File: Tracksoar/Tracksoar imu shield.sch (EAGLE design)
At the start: 12 parts, among them U1 HEX_CONVERTER, U2 LSM9DS1

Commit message: removed old shields
removed square shields and added values to shield passives
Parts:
- C1: value (none) -> 10uf
- C2, C3, C5: value (none) -> .1uf
- C4: value (none) -> 10nf
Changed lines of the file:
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@@
 <part name="U1" library="SparkFun-DigitalIC" deviceset="HEX_CONVERTER" device=""/>
 <part name="U2" library="SparkFun-Sensors" deviceset="LSM9DS1" device=""/>
-<part name="C1" library="SparkFun-Passives" deviceset="CAP" device="0805"/>
-<part name="C2" library="SparkFun-Passives" deviceset="CAP" device="0805"/>
-<part name="C3" library="SparkFun-Passives" deviceset="CAP" device="0805"/>
-<part name="C4" library="SparkFun-Passives" deviceset="CAP" device="0805"/>
-<part name="C5" library="SparkFun-Passives" deviceset="CAP" device="0805"/>
+<part name="C1" library="SparkFun-Passives" deviceset="CAP" device="0805" value="10uf"/>
+<part name="C2" library="SparkFun-Passives" deviceset="CAP" device="0805" value=".1uf"/>
+<part name="C3" library="SparkFun-Passives" deviceset="CAP" device="0805" value=".1uf"/>
+<part name="C4" library="SparkFun-Passives" deviceset="CAP" device="0805" value="10nf"/>
+<part name="C5" library="SparkFun-Passives" deviceset="CAP" device="0805" value=".1uf"/>
 <part name="U$2" library="SparkFun-PowerIC" deviceset="LM3480IM4" device=""/>
 </parts>
@@
 <junction x="63.5" y="60.96"/>
 <pinref part="C5" gate="G$1" pin="2"/>
-<wire x1="71.12" y1="60.96" x2="73.66" y2="60.96" width="0.1524" layer="91"/>
+<wire x1="71.12" y1="60.96" x2="78.74" y2="60.96" width="0.1524" layer="91"/>
 <junction x="71.12" y="60.96"/>
 <junction x="40.64" y="60.96"/>
-<label x="73.66" y="60.96" size="1.778" layer="95"/>
+<label x="78.74" y="60.96" size="1.778" layer="95"/>
 </segment>
 </net>

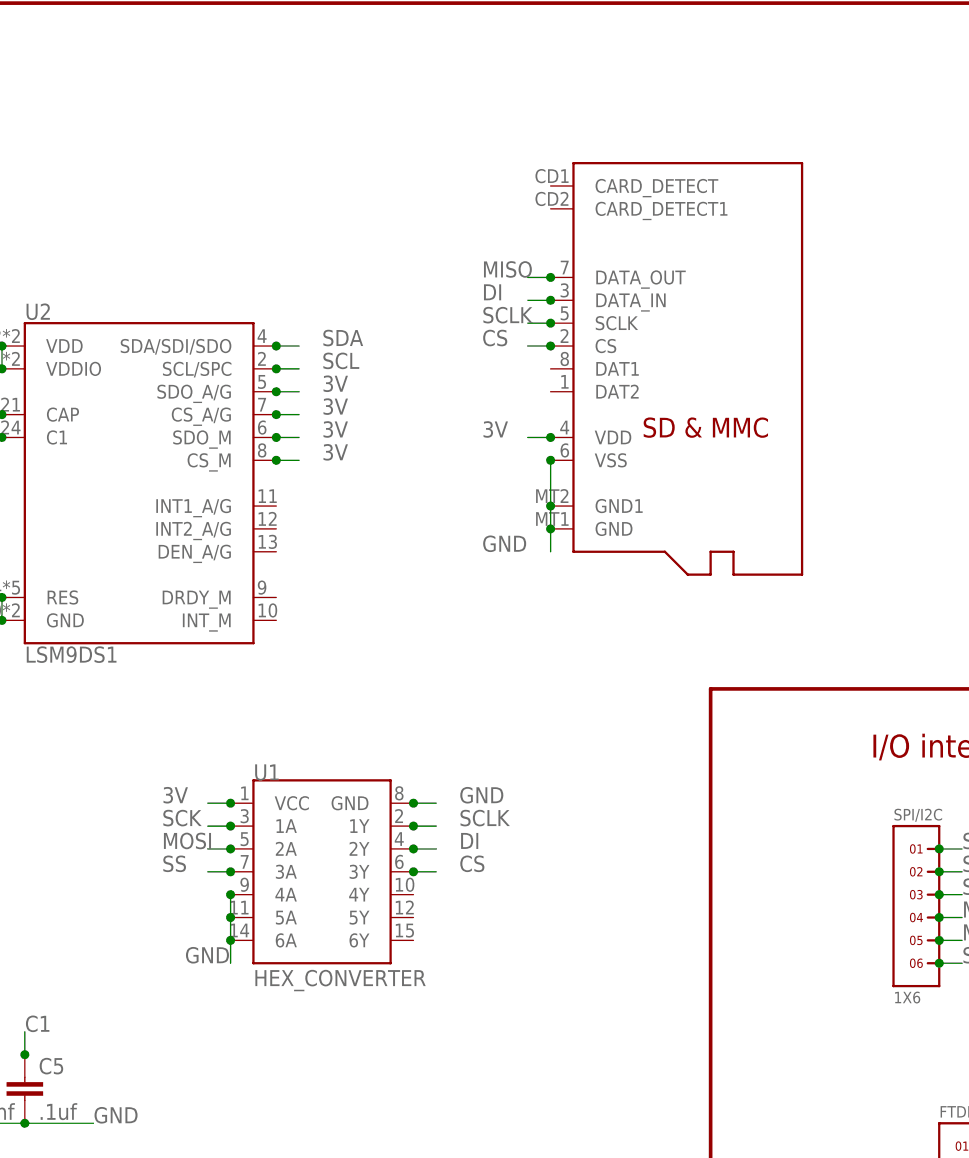
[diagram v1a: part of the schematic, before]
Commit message: replaced sd with eeprom
the atmega328p does not have enough SRAM to handle the Trackuino duties
and SD read / write. It has been replace with an ST Micro M24M02 2Mb
eeprom. This will result in much less RAM usage, a smaller BOM, lower
cost, and lower power usage. However it also means we lose portability
of storage and easy computer interfacing. We’ll look at revising this
in future versions.
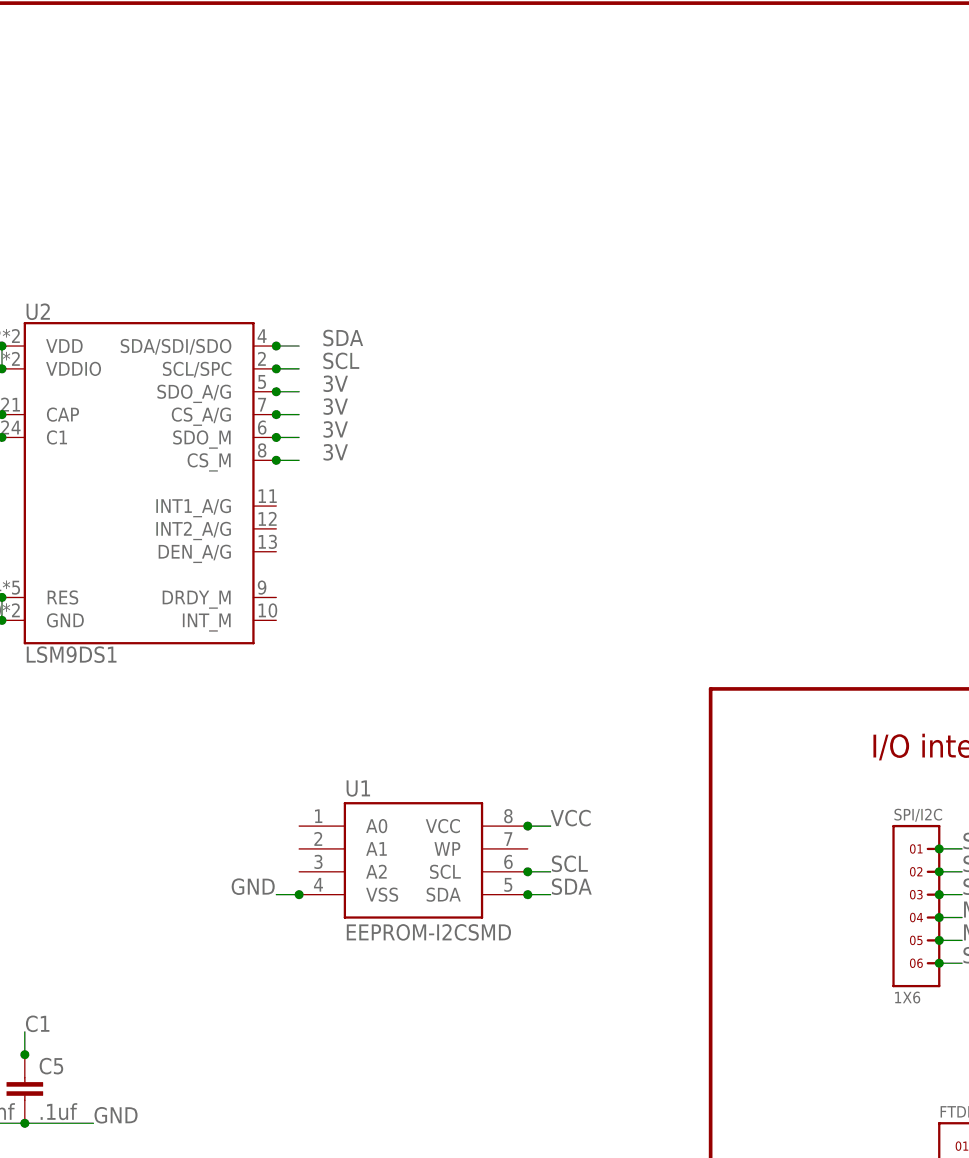
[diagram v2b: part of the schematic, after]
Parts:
- removed U$1: MICROSD, adafruit:MICROSD
- U1: value HEX_CONVERTER -> EEPROM-I2CSMD; device SparkFun-DigitalIC:HEX_CONVERTER -> SparkFun-DigitalIC:EEPROM-I2CSMD
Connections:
- removed net CS: U$1.CS, U1.3Y
- removed net DI: U$1.DATA_IN, U1.2Y
- removed net SCLK: U$1.SCLK, U1.1Y
- net 3V: no longer U$1.VDD, U1.VCC
- net GND: now also U1.VSS; no longer U$1.GND, U$1.GND1, U$1.VSS, U1.4A, U1.5A, U1.6A, U1.GND
- net MISO: no longer U$1.DATA_OUT
- net MOSI: no longer U1.2A
- net SCK: no longer U1.1A
- net SCL: now also U1.SCL
- net SDA: now also U1.SDA
- net SS: no longer U1.3A
- net VCC: now also U1.VCC
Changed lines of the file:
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@@
 <layers>
 <layer number="1" name="Top" color="4" fill="1" visible="no" active="no"/>
+<layer number="2" name="Route2" color="1" fill="3" visible="no" active="no"/>
+<layer number="3" name="Route3" color="4" fill="3" visible="no" active="no"/>
+<layer number="14" name="Route14" color="1" fill="6" visible="no" active="no"/>
+<layer number="15" name="Route15" color="4" fill="6" visible="no" active="no"/>
 <layer number="16" name="Bottom" color="1" fill="1" visible="no" active="no"/>
 <layer number="17" name="Pads" color="2" fill="1" visible="no" active="no"/>
@@
 <part name="FTDI" library="headers(2mm)" deviceset="1X7" device=""/>
 <part name="SPI/I2C" library="headers(2mm)" deviceset="1X6" device=""/>
-<part name="U$1" library="adafruit" deviceset="MICROSD" device=""/>
-<part name="U1" library="SparkFun-DigitalIC" deviceset="HEX_CONVERTER" device=""/>
 <part name="U2" library="SparkFun-Sensors" deviceset="LSM9DS1" device=""/>
 <part name="C1" library="SparkFun-Passives" deviceset="CAP" device="0805" value="10uf"/>
@@
 <part name="C5" library="SparkFun-Passives" deviceset="CAP" device="0805" value=".1uf"/>
 <part name="U$2" library="SparkFun-PowerIC" deviceset="LM3480IM4" device=""/>
+<part name="U1" library="SparkFun-DigitalIC" deviceset="EEPROM-I2C" device="SMD"/>
 </parts>
 <sheets>
@@
 <instance part="FTDI" gate="G$1" x="175.26" y="50.8"/>
 <instance part="SPI/I2C" gate="G$1" x="170.18" y="83.82"/>
-<instance part="U$1" gate="G$1" x="147.32" y="147.32"/>
-<instance part="U1" gate="G$1" x="104.14" y="88.9"/>
 <instance part="U2" gate="G$1" x="83.82" y="132.08"/>
 <instance part="C1" gate="G$1" x="40.64" y="63.5"/>
@@
 <instance part="C5" gate="G$1" x="71.12" y="63.5"/>
 <instance part="U$2" gate="G$1" x="223.52" y="81.28"/>
+<instance part="U1" gate="G$1" x="114.3" y="88.9"/>
 </instances>
 <busses>
@@
 <junction x="68.58" y="116.84"/>
 <label x="60.96" y="116.84" size="1.778" layer="95"/>
-</segment>
-<segment>
-<pinref part="U1" gate="G$1" pin="4A"/>
-<wire x1="93.98" y1="86.36" x2="93.98" y2="83.82" width="0.1524" layer="91"/>
-<pinref part="U1" gate="G$1" pin="5A"/>
-<junction x="93.98" y="83.82"/>
-<wire x1="93.98" y1="83.82" x2="93.98" y2="81.28" width="0.1524" layer="91"/>
-<junction x="93.98" y="86.36"/>
-<pinref part="U1" gate="G$1" pin="6A"/>
-<junction x="93.98" y="81.28"/>
-<wire x1="93.98" y1="81.28" x2="93.98" y2="78.74" width="0.1524" layer="91"/>
-<label x="88.9" y="78.74" size="1.778" layer="95"/>
-</segment>
-<segment>
-<pinref part="U1" gate="G$1" pin="GND"/>
-<wire x1="114.3" y1="96.52" x2="116.84" y2="96.52" width="0.1524" layer="91"/>
-<junction x="114.3" y="96.52"/>
-<label x="119.38" y="96.52" size="1.778" layer="95"/>
-</segment>
-<segment>
-<pinref part="U$1" gate="G$1" pin="VSS"/>
-<wire x1="129.54" y1="134.62" x2="129.54" y2="129.54" width="0.1524" layer="91"/>
-<pinref part="U$1" gate="G$1" pin="GND"/>
-<junction x="129.54" y="127"/>
-<wire x1="129.54" y1="129.54" x2="129.54" y2="127" width="0.1524" layer="91"/>
-<wire x1="129.54" y1="127" x2="129.54" y2="124.46" width="0.1524" layer="91"/>
-<pinref part="U$1" gate="G$1" pin="GND1"/>
-<junction x="129.54" y="129.54"/>
-<junction x="129.54" y="134.62"/>
-<label x="121.92" y="124.46" size="1.778" layer="95"/>
 </segment>
 <segment>
@@
 <label x="78.74" y="60.96" size="1.778" layer="95"/>
 </segment>
+<segment>
+<pinref part="U1" gate="G$1" pin="VSS"/>
+<wire x1="101.6" y1="86.36" x2="99.06" y2="86.36" width="0.1524" layer="91"/>
+<junction x="101.6" y="86.36"/>
+<label x="93.98" y="86.36" size="1.778" layer="95"/>
+</segment>
 </net>
 <net name="VCC" class="0">
@@
 <label x="203.2" y="81.28" size="1.778" layer="95"/>
 </segment>
+<segment>
+<pinref part="U1" gate="G$1" pin="VCC"/>
+<wire x1="127" y1="93.98" x2="129.54" y2="93.98" width="0.1524" layer="91"/>
+<junction x="127" y="93.98"/>
+<label x="129.54" y="93.98" size="1.778" layer="95"/>
+</segment>
 </net>
 <net name="DTR" class="0">
@@
 <junction x="172.72" y="83.82"/>
 </segment>
-<segment>
-<pinref part="U$1" gate="G$1" pin="DATA_OUT"/>
-<wire x1="129.54" y1="154.94" x2="127" y2="154.94" width="0.1524" layer="91"/>
-<junction x="129.54" y="154.94"/>
-<label x="121.92" y="154.94" size="1.778" layer="95"/>
-</segment>
 </net>
 <net name="MOSI" class="0">
@@
 <junction x="172.72" y="81.28"/>
 </segment>
-<segment>
-<pinref part="U1" gate="G$1" pin="2A"/>
-<wire x1="93.98" y1="91.44" x2="91.44" y2="91.44" width="0.1524" layer="91"/>
-<junction x="93.98" y="91.44"/>
-<label x="86.36" y="91.44" size="1.778" layer="95"/>
-</segment>
 </net>
 <net name="SCK" class="0">
@@
 <junction x="172.72" y="86.36"/>
 </segment>
-<segment>
-<pinref part="U1" gate="G$1" pin="1A"/>
-<wire x1="93.98" y1="93.98" x2="91.44" y2="93.98" width="0.1524" layer="91"/>
-<junction x="93.98" y="93.98"/>
-<label x="86.36" y="93.98" size="1.778" layer="95"/>
-</segment>
 </net>
 <net name="SS" class="0">
@@
 <junction x="172.72" y="78.74"/>
 </segment>
-<segment>
-<pinref part="U1" gate="G$1" pin="3A"/>
-<wire x1="93.98" y1="88.9" x2="91.44" y2="88.9" width="0.1524" layer="91"/>
-<junction x="93.98" y="88.9"/>
-<label x="86.36" y="88.9" size="1.778" layer="95"/>
-</segment>
 </net>
 <net name="SDA" class="0">
@@
 <label x="104.14" y="147.32" size="1.778" layer="95"/>
 </segment>
+<segment>
+<pinref part="U1" gate="G$1" pin="SDA"/>
+<wire x1="127" y1="86.36" x2="129.54" y2="86.36" width="0.1524" layer="91"/>
+<junction x="127" y="86.36"/>
+<label x="129.54" y="86.36" size="1.778" layer="95"/>
+</segment>
 </net>
 <net name="SCL" class="0">
@@
 <junction x="99.06" y="144.78"/>
 <label x="104.14" y="144.78" size="1.778" layer="95"/>
+</segment>
+<segment>
+<pinref part="U1" gate="G$1" pin="SCL"/>
+<wire x1="127" y1="88.9" x2="129.54" y2="88.9" width="0.1524" layer="91"/>
+<junction x="127" y="88.9"/>
+<label x="129.54" y="88.9" size="1.778" layer="95"/>
 </segment>
 </net>
@@
 </segment>
 <segment>
-<pinref part="U1" gate="G$1" pin="VCC"/>
-<wire x1="93.98" y1="96.52" x2="91.44" y2="96.52" width="0.1524" layer="91"/>
-<junction x="93.98" y="96.52"/>
-<label x="86.36" y="96.52" size="1.778" layer="95"/>
-</segment>
-<segment>
-<pinref part="U$1" gate="G$1" pin="VDD"/>
-<wire x1="129.54" y1="137.16" x2="127" y2="137.16" width="0.1524" layer="91"/>
-<junction x="129.54" y="137.16"/>
-<label x="121.92" y="137.16" size="1.778" layer="95"/>
-</segment>
-<segment>
 <pinref part="U$2" gate="G$1" pin="OUT"/>
 <wire x1="236.22" y1="81.28" x2="238.76" y2="81.28" width="0.1524" layer="91"/>
@@
 </segment>
 </net>
-<net name="SCLK" class="0">
-<segment>
-<pinref part="U1" gate="G$1" pin="1Y"/>
-<wire x1="114.3" y1="93.98" x2="116.84" y2="93.98" width="0.1524" layer="91"/>
-<junction x="114.3" y="93.98"/>
-<label x="119.38" y="93.98" size="1.778" layer="95"/>
-</segment>
-<segment>
-<pinref part="U$1" gate="G$1" pin="SCLK"/>
-<wire x1="129.54" y1="149.86" x2="127" y2="149.86" width="0.1524" layer="91"/>
-<junction x="129.54" y="149.86"/>
-<label x="121.92" y="149.86" size="1.778" layer="95"/>
-</segment>
-</net>
-<net name="DI" class="0">
-<segment>
-<pinref part="U1" gate="G$1" pin="2Y"/>
-<wire x1="114.3" y1="91.44" x2="116.84" y2="91.44" width="0.1524" layer="91"/>
-<junction x="114.3" y="91.44"/>
-<label x="119.38" y="91.44" size="1.778" layer="95"/>
-</segment>
-<segment>
-<pinref part="U$1" gate="G$1" pin="DATA_IN"/>
-<wire x1="129.54" y1="152.4" x2="127" y2="152.4" width="0.1524" layer="91"/>
-<junction x="129.54" y="152.4"/>
-<label x="121.92" y="152.4" size="1.778" layer="95"/>
-</segment>
-</net>
-<net name="CS" class="0">
-<segment>
-<pinref part="U1" gate="G$1" pin="3Y"/>
-<wire x1="114.3" y1="88.9" x2="116.84" y2="88.9" width="0.1524" layer="91"/>
-<junction x="114.3" y="88.9"/>
-<label x="119.38" y="88.9" size="1.778" layer="95"/>
-</segment>
-<segment>
-<pinref part="U$1" gate="G$1" pin="CS"/>
-<wire x1="129.54" y1="147.32" x2="127" y2="147.32" width="0.1524" layer="91"/>
-<junction x="129.54" y="147.32"/>
-<label x="121.92" y="147.32" size="1.778" layer="95"/>
-</segment>
-</net>
